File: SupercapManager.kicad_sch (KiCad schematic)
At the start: 10 parts, among them J1 JST4_F, J2 XT30_F, J3 XT30_F, J4 XT30_F, J5 XT30_F, J9 XT30_F, Q1 BSC059N04LS6, Q2 BSC059N04LS6

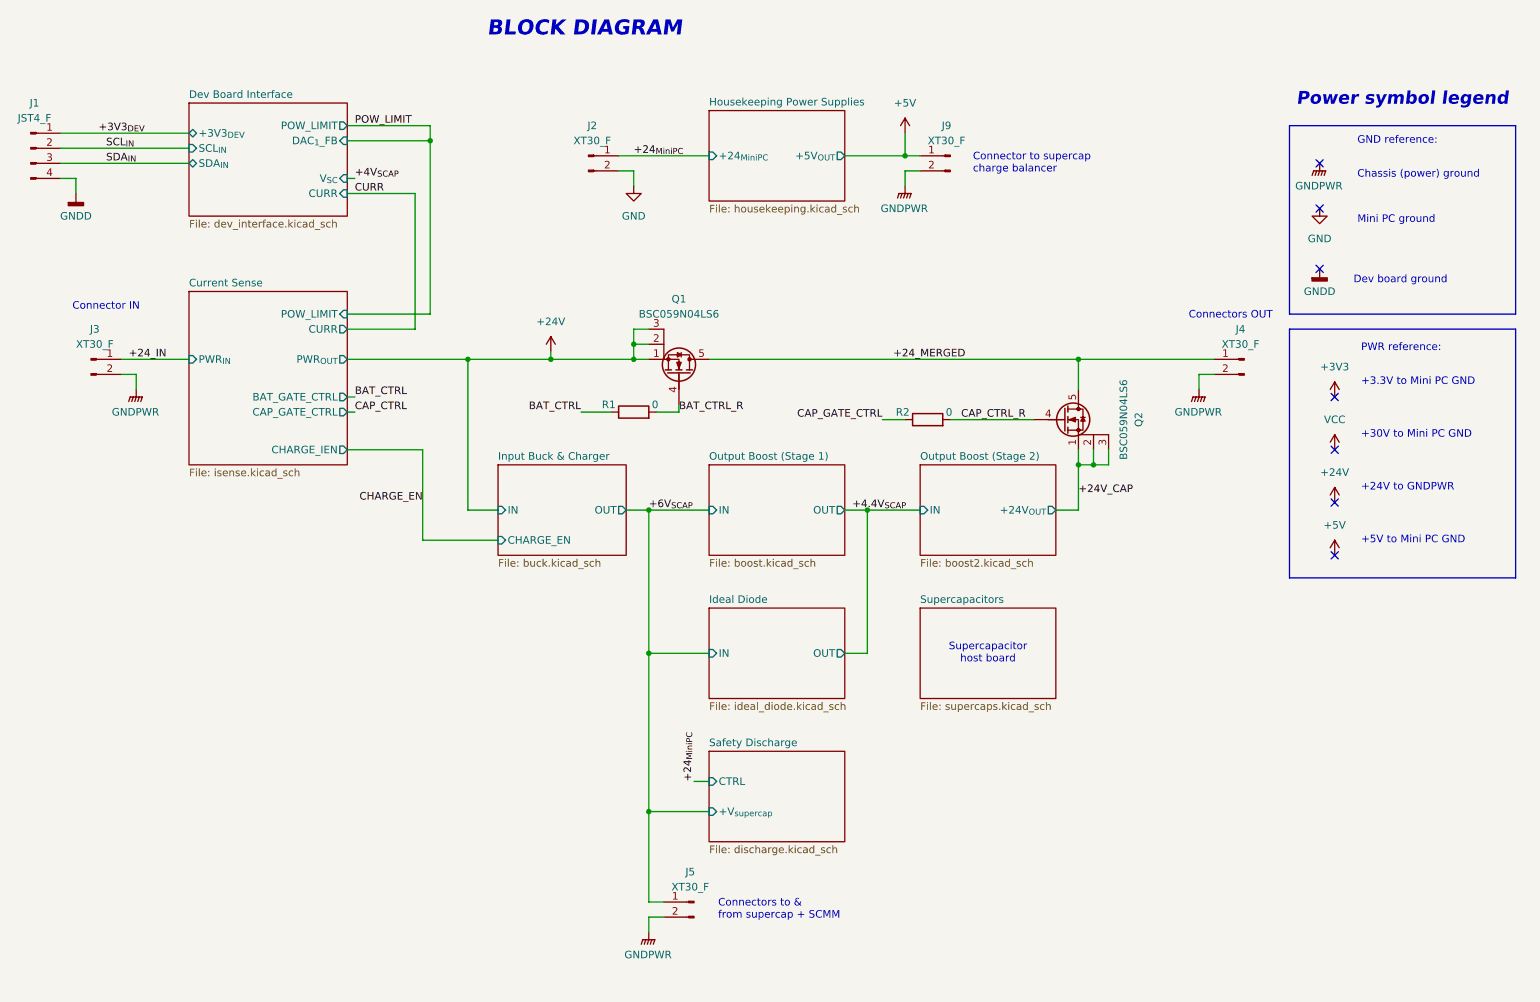
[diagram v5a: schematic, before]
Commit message: Renumbering components
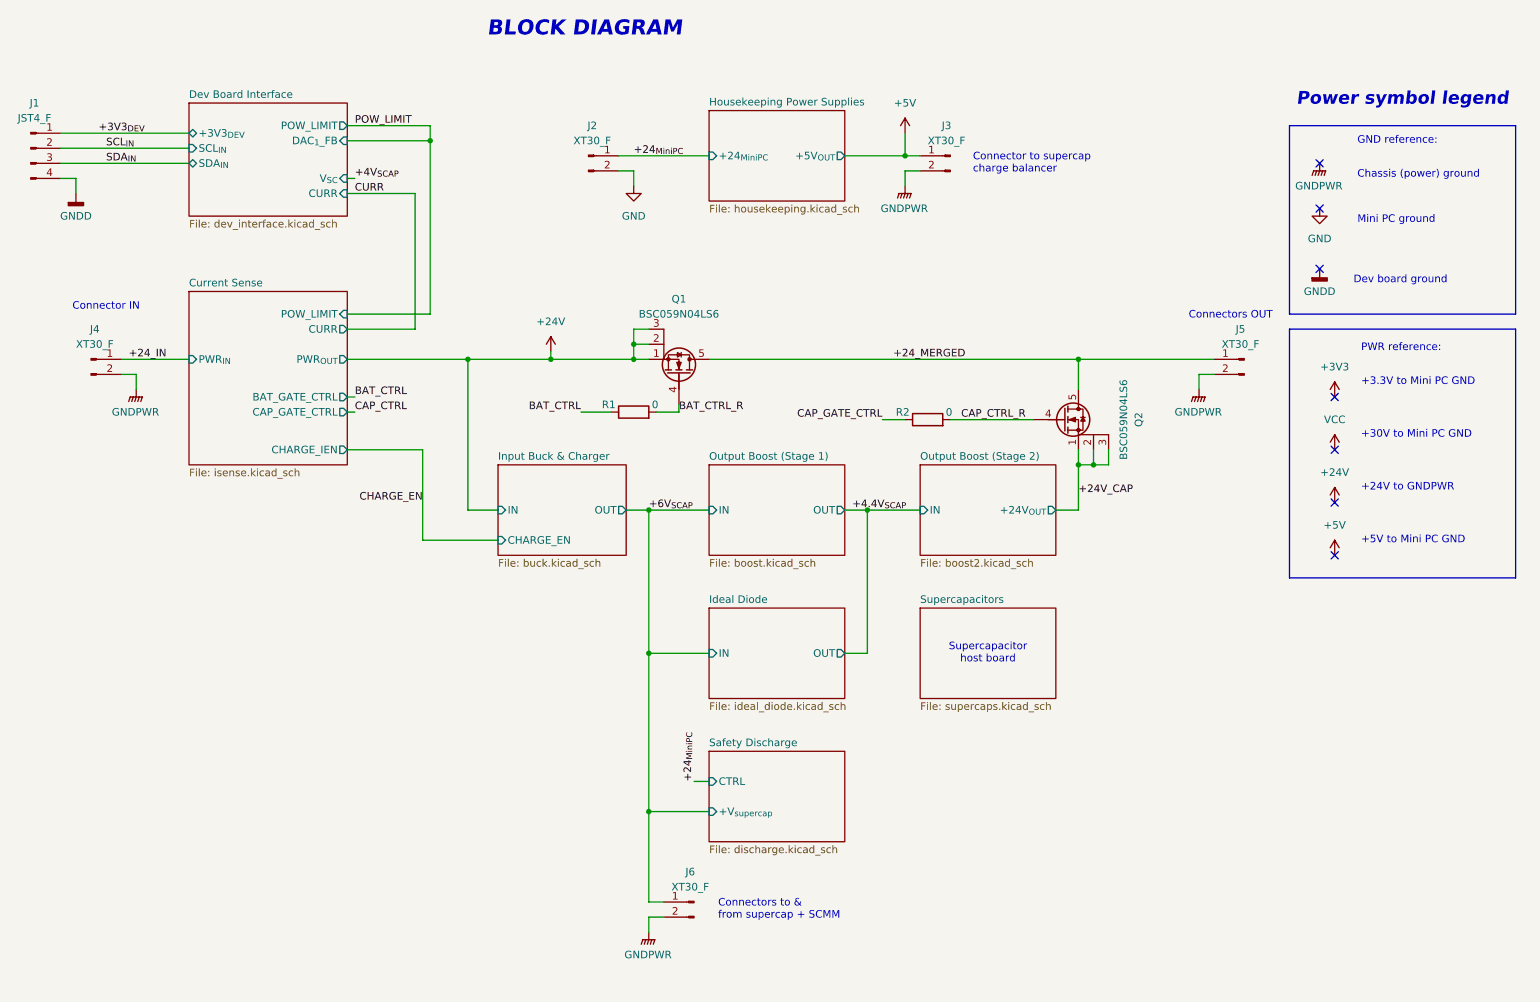
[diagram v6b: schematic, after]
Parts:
- renumbered J9 to J3, J3 to J4, J4 to J5, J5 to J6
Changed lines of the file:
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@@
 		(dnp no)
 		(fields_autoplaced yes)
-		(property "Reference" "J9"
+		(property "Reference" "J3"
 			(at 175.895 40.64 0)
 			(effects
@@
 			(project "SupercapManager"
 				(path "/6197145b-e7d4-44cc-9d90-537b6501bf60"
-					(reference "J9")
+					(reference "J3")
 					(unit 1)
 				)
@@
 		(dnp no)
 		(fields_autoplaced yes)
-		(property "Reference" "#PWR07"
+		(property "Reference" "#PWR09"
 			(at 39.37 90.17 0)
 			(effects
@@
 			(project "SupercapManager"
 				(path "/6197145b-e7d4-44cc-9d90-537b6501bf60"
-					(reference "#PWR07")
+					(reference "#PWR09")
 					(unit 1)
 				)
@@
 		(dnp no)
 		(fields_autoplaced yes)
-		(property "Reference" "#PWR05"
+		(property "Reference" "#PWR07"
 			(at 238.76 71.12 0)
 			(effects
@@
 			(project ""
 				(path "/6197145b-e7d4-44cc-9d90-537b6501bf60"
-					(reference "#PWR05")
+					(reference "#PWR07")
 					(unit 1)
 				)
@@
 		(dnp no)
 		(fields_autoplaced yes)
-		(property "Reference" "#PWR094"
+		(property "Reference" "#PWR04"
 			(at 168.91 55.88 0)
 			(effects
@@
 			(project "SupercapManager"
 				(path "/6197145b-e7d4-44cc-9d90-537b6501bf60"
-					(reference "#PWR094")
+					(reference "#PWR04")
 					(unit 1)
 				)
@@
 		(dnp no)
 		(fields_autoplaced yes)
-		(property "Reference" "#PWR03"
+		(property "Reference" "#PWR05"
 			(at 29.21 58.42 0)
 			(effects
@@
 			(project "SupercapManager"
 				(path "/6197145b-e7d4-44cc-9d90-537b6501bf60"
-					(reference "#PWR03")
+					(reference "#PWR05")
 					(unit 1)
 				)
@@
 		(dnp no)
 		(fields_autoplaced yes)
-		(property "Reference" "#PWR0106"
+		(property "Reference" "#PWR01"
 			(at 168.91 45.72 0)
 			(effects
@@
 			(project ""
 				(path "/6197145b-e7d4-44cc-9d90-537b6501bf60"
-					(reference "#PWR0106")
+					(reference "#PWR01")
 					(unit 1)
 				)
@@
 		(dnp no)
 		(fields_autoplaced yes)
-		(property "Reference" "#PWR02"
+		(property "Reference" "#PWR03"
 			(at 123.19 57.15 0)
 			(effects
@@
 			(project ""
 				(path "/6197145b-e7d4-44cc-9d90-537b6501bf60"
-					(reference "#PWR02")
+					(reference "#PWR03")
 					(unit 1)
 				)
@@
 		(dnp no)
 		(fields_autoplaced yes)
-		(property "Reference" "#PWR09"
+		(property "Reference" "#PWR011"
 			(at 241.3 90.17 0)
 			(effects
@@
 			(project ""
 				(path "/6197145b-e7d4-44cc-9d90-537b6501bf60"
-					(reference "#PWR09")
+					(reference "#PWR011")
 					(unit 1)
 				)
@@
 		(dnp no)
 		(fields_autoplaced yes)
-		(property "Reference" "#PWR010"
+		(property "Reference" "#PWR012"
 			(at 241.3 99.06 0)
 			(effects
@@
 			(project ""
 				(path "/6197145b-e7d4-44cc-9d90-537b6501bf60"
-					(reference "#PWR010")
+					(reference "#PWR012")
 					(unit 1)
 				)
@@
 		(on_board yes)
 		(dnp no)
-		(property "Reference" "J5"
+		(property "Reference" "J6"
 			(at 132.715 166.37 0)
 			(effects
@@
 			(project "SupercapManager"
 				(path "/6197145b-e7d4-44cc-9d90-537b6501bf60"
-					(reference "J5")
+					(reference "J6")
 					(unit 1)
 				)
@@
 		(dnp no)
 		(fields_autoplaced yes)
-		(property "Reference" "#PWR08"
+		(property "Reference" "#PWR010"
 			(at 218.44 90.17 0)
 			(effects
@@
 			(project "SupercapManager"
 				(path "/6197145b-e7d4-44cc-9d90-537b6501bf60"
-					(reference "#PWR08")
+					(reference "#PWR010")
 					(unit 1)
 				)
@@
 		(dnp no)
 		(fields_autoplaced yes)
-		(property "Reference" "#PWR06"
+		(property "Reference" "#PWR08"
 			(at 109.22 82.55 0)
 			(effects
@@
 			(project ""
 				(path "/6197145b-e7d4-44cc-9d90-537b6501bf60"
-					(reference "#PWR06")
+					(reference "#PWR08")
 					(unit 1)
 				)
@@
 		(dnp no)
 		(fields_autoplaced yes)
-		(property "Reference" "#PWR013"
+		(property "Reference" "#PWR015"
 			(at 125.73 181.61 0)
 			(effects
@@
 			(project "SupercapManager"
 				(path "/6197145b-e7d4-44cc-9d90-537b6501bf60"
-					(reference "#PWR013")
+					(reference "#PWR015")
 					(unit 1)
 				)
@@
 		(dnp no)
 		(fields_autoplaced yes)
-		(property "Reference" "#PWR011"
+		(property "Reference" "#PWR013"
 			(at 241.3 107.95 0)
 			(effects
@@
 			(project ""
 				(path "/6197145b-e7d4-44cc-9d90-537b6501bf60"
-					(reference "#PWR011")
+					(reference "#PWR013")
 					(unit 1)
 				)
@@
 		(dnp no)
 		(fields_autoplaced yes)
-		(property "Reference" "J3"
+		(property "Reference" "J4"
 			(at 32.385 74.93 0)
 			(effects
@@
 			(project ""
 				(path "/6197145b-e7d4-44cc-9d90-537b6501bf60"
-					(reference "J3")
+					(reference "J4")
 					(unit 1)
 				)
@@
 		(dnp no)
 		(fields_autoplaced yes)
-		(property "Reference" "#PWR0107"
+		(property "Reference" "#PWR014"
 			(at 241.3 116.84 0)
 			(effects
@@
 			(project "SupercapManager"
 				(path "/6197145b-e7d4-44cc-9d90-537b6501bf60"
-					(reference "#PWR0107")
+					(reference "#PWR014")
 					(unit 1)
 				)
@@
 		(on_board yes)
 		(dnp no)
-		(property "Reference" "J4"
+		(property "Reference" "J5"
 			(at 225.425 74.93 0)
 			(effects
@@
 			(project "SupercapManager"
 				(path "/6197145b-e7d4-44cc-9d90-537b6501bf60"
-					(reference "J4")
+					(reference "J5")
 					(unit 1)
 				)
@@
 		(dnp no)
 		(fields_autoplaced yes)
-		(property "Reference" "#PWR04"
+		(property "Reference" "#PWR06"
 			(at 238.76 60.96 0)
 			(effects
@@
 			(project ""
 				(path "/6197145b-e7d4-44cc-9d90-537b6501bf60"
-					(reference "#PWR04")
+					(reference "#PWR06")
 					(unit 1)
 				)
@@
 		(dnp no)
 		(fields_autoplaced yes)
-		(property "Reference" "#PWR01"
+		(property "Reference" "#PWR02"
 			(at 238.76 52.07 0)
 			(effects
@@
 			(project ""
 				(path "/6197145b-e7d4-44cc-9d90-537b6501bf60"
-					(reference "#PWR01")
-					(unit 1)
-				)
+					(reference "#PWR02")
+					(unit 1)
+				)

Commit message: Add voltage ratings to capacitors & respec caps to not explode
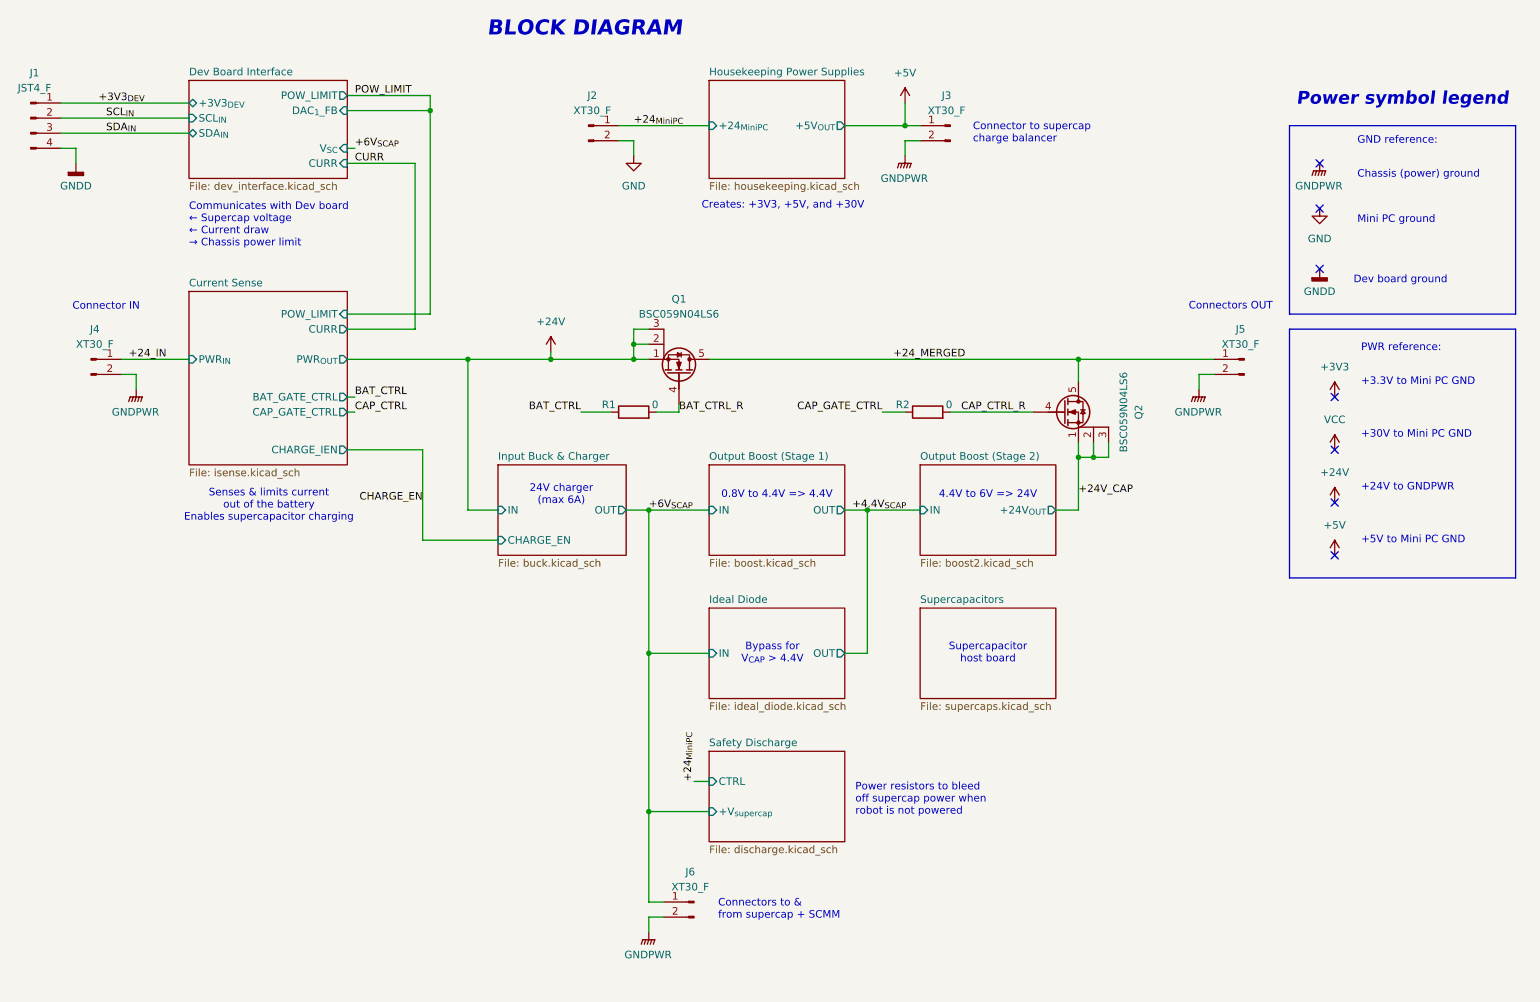
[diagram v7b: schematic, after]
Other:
- note added: "0.8V to 4.4V => 4.4V"
- note added: "24V charger (max 6A)"
- note added: "4.4V to 6V => 24V"
- note added: "Bypass for V_{CAP} > 4.4V"
- note added: "Communicates with Dev board ← Supercap voltage ← Current draw → Chassis power limit"
- note added: "Creates: +3V3, +5V, and +30V"
- note added: "Power resistors to bleed off supercap power when robot is not powered"
- note added: "Senses & limits current out of the battery Enables supercapacitor charging"
- moved on the sheet: J1, J2, J3, Q2, R2

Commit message: Specc'd all components + started creating rev 1b boards
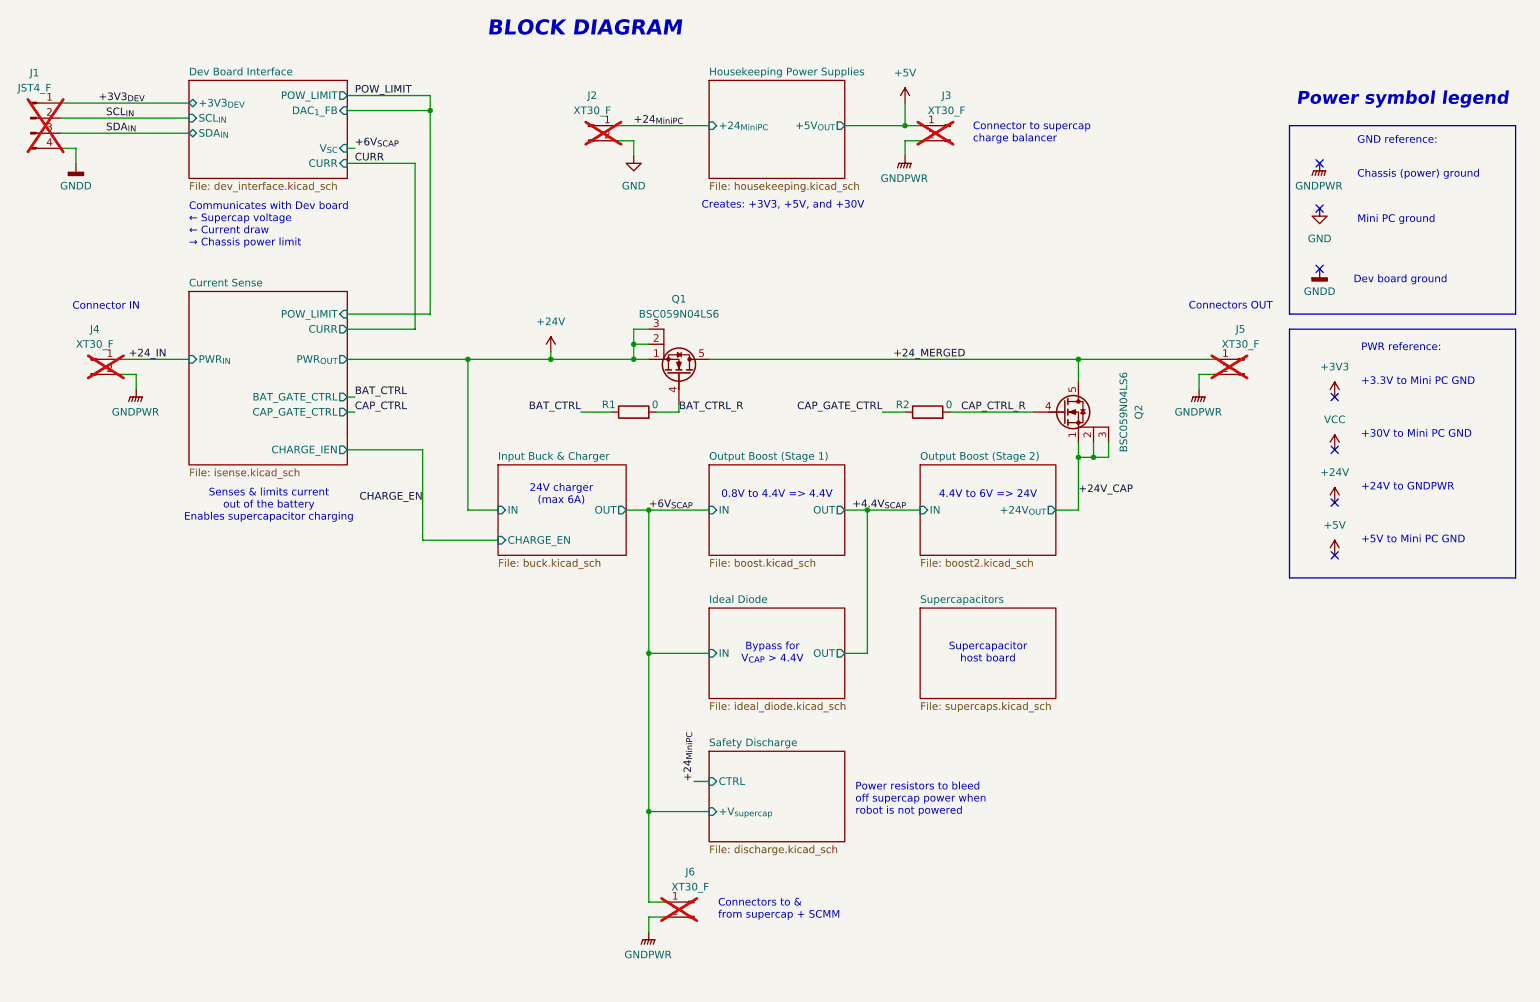
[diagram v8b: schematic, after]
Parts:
- J1, J2, J3, J4, J5, J6: now not fitted
- R1, R2: Mouser Part Number (none) -> 660-RK73Z1JTTDD
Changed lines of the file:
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@@
 		(in_bom yes)
 		(on_board yes)
-		(dnp no)
+		(dnp yes)
 		(fields_autoplaced yes)
 		(property "Reference" "J3"
@@
 			)
 		)
+		(property "Mouser Part Number" "660-RK73Z1JTTDD"
+			(at 172.72 88.9 0)
+			(effects
+				(font
+					(size 1.27 1.27)
+				)
+				(hide yes)
+			)
+		)
 		(pin "2"
 		)
@@
 			)
 		)
+		(property "Mouser Part Number" "660-RK73Z1JTTDD"
+			(at 123.19 88.9 0)
+			(effects
+				(font
+					(size 1.27 1.27)
+				)
+				(hide yes)
+			)
+		)
 		(pin "2"
 		)
@@
 		(in_bom yes)
 		(on_board yes)
-		(dnp no)
+		(dnp yes)
 		(property "Reference" "J6"
 			(at 132.715 166.37 0)
@@
 		(in_bom yes)
 		(on_board yes)
-		(dnp no)
+		(dnp yes)
 		(fields_autoplaced yes)
 		(property "Reference" "J2"
@@
 		(in_bom yes)
 		(on_board yes)
-		(dnp no)
+		(dnp yes)
 		(fields_autoplaced yes)
 		(property "Reference" "J4"
@@
 		(in_bom yes)
 		(on_board yes)
-		(dnp no)
+		(dnp yes)
 		(fields_autoplaced yes)
 		(property "Reference" "J1"
@@
 		(in_bom yes)
 		(on_board yes)
-		(dnp no)
+		(dnp yes)
 		(property "Reference" "J5"
 			(at 225.425 74.93 0)
